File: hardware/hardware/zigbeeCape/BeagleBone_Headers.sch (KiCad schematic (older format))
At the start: 2 parts, among them U4 BeagleBone_P8, U5 BeagleBone_P9

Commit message: Fixing Git issue
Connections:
- net LAN_Heartbeat: now also U5.41 (GPIO_20); no longer U5.15 (GPIO_48)
- net Network_Connect: now also U5.15 (GPIO_48); no longer U5.41 (GPIO_20)
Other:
- note removed: "Random GPIO pin chozen."
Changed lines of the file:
@@
 	1    0    0    -1
 $EndComp
-Text HLabel 5300 2250 0    50   Input ~ 0
+Text HLabel 5650 2250 0    50   Input ~ 0
 BeagleBone_Reset
-Text HLabel 4700 850  0    50   Output ~ 0
+Text HLabel 7300 1550 2    50   Output ~ 0
 LAN_Heartbeat
-Text HLabel 4700 950  0    50   Input ~ 0
+Text HLabel 7300 1650 2    50   Input ~ 0
 Network_Connect
-Text HLabel 5250 3650 0    50   Input ~ 0
+Text HLabel 5650 3650 0    50   Input ~ 0
 UART_TX
-Text HLabel 7500 3150 2    50   Input ~ 0
+Text HLabel 7250 3150 2    50   Input ~ 0
 SPI_MISO
-Text HLabel 7500 3250 2    50   Output ~ 0
+Text HLabel 7250 3250 2    50   Output ~ 0
 SPI_MOSI
-Text HLabel 7500 3350 2    50   Output ~ 0
+Text HLabel 7250 3350 2    50   Output ~ 0
 SPI_CS
-Text HLabel 7500 3050 2    50   Output ~ 0
+Text HLabel 7250 3050 2    50   Output ~ 0
 SPI_CLK
-Text HLabel 7500 3950 2    50   Output ~ 0
+Text HLabel 7250 3950 2    50   Output ~ 0
 I2C2_SCL
-Text HLabel 7500 3850 2    50   BiDi ~ 0
+Text HLabel 7250 3850 2    50   BiDi ~ 0
 I2C2_SDA
-Wire Wire Line
-	5800 2250 5300 2250
-Text HLabel 5250 3750 0    50   Output ~ 0
+Text HLabel 5650 3750 0    50   Output ~ 0
 UART_RX
-Wire Wire Line
-	5800 3750 5250 3750
-Wire Wire Line
-	5250 3650 5800 3650
-Wire Wire Line
-	7100 3950 7500 3950
-Wire Wire Line
-	7500 3850 7100 3850
-Wire Wire Line
-	7500 3350 7100 3350
-Wire Wire Line
-	7100 3250 7500 3250
-Wire Wire Line
-	7500 3150 7100 3150
-Wire Wire Line
-	7500 3050 7100 3050
-Text Notes 5100 800  0    50   ~ 0
-Random GPIO pin chozen.
-Text Notes 5100 1050 0    50   ~ 0
-Random GPIO pin chozen.
-Wire Wire Line
-	2250 1550 1450 1550
-Wire Wire Line
-	1450 1550 1450 1650
-Wire Wire Line
-	5800 1650 5300 1650
-Wire Wire Line
-	5300 1550 5300 1650
-Wire Wire Line
-	5800 2400 5200 2400
-Wire Wire Line
-	5200 2400 5200 2500
-Connection ~ 5200 2500
 $Comp
 L power:GND #PWR046
 U 1 1 608F7A9D
-P 1450 1800
-F 0 "#PWR046" H 1450 1550 50  0001 C CNN
-F 1 "GND" H 1455 1627 50  0000 C CNN
-F 2 "" H 1450 1800 50  0001 C CNN
-F 3 "" H 1450 1800 50  0001 C CNN
-	1    1450 1800
+P 2050 1750
+F 0 "#PWR046" H 2050 1500 50  0001 C CNN
+F 1 "GND" H 2055 1577 50  0000 C CNN
+F 2 "" H 2050 1750 50  0001 C CNN
+F 3 "" H 2050 1750 50  0001 C CNN
+	1    2050 1750
 	1    0    0    -1
 $EndComp
@@
 L power:GND #PWR047
 U 1 1 608F7F64
-P 4800 2550
-F 0 "#PWR047" H 4800 2300 50  0001 C CNN
-F 1 "GND" H 4805 2377 50  0000 C CNN
-F 2 "" H 4800 2550 50  0001 C CNN
-F 3 "" H 4800 2550 50  0001 C CNN
-	1    4800 2550
+P 5650 2950
+F 0 "#PWR047" H 5650 2700 50  0001 C CNN
+F 1 "GND" H 5655 2777 50  0000 C CNN
+F 2 "" H 5650 2950 50  0001 C CNN
+F 3 "" H 5650 2950 50  0001 C CNN
+	1    5650 2950
 	1    0    0    -1
 $EndComp
@@
 L power:+3.3V #PWR048
 U 1 1 608FAB4C
-P 5300 1500
-F 0 "#PWR048" H 5300 1350 50  0001 C CNN
-F 1 "+3.3V" H 5315 1673 50  0000 C CNN
-F 2 "" H 5300 1500 50  0001 C CNN
-F 3 "" H 5300 1500 50  0001 C CNN
-	1    5300 1500
+P 5650 1450
+F 0 "#PWR048" H 5650 1300 50  0001 C CNN
+F 1 "+3.3V" H 5665 1623 50  0000 C CNN
+F 2 "" H 5650 1450 50  0001 C CNN
+F 3 "" H 5650 1450 50  0001 C CNN
+	1    5650 1450
 	1    0    0    -1
 $EndComp
@@
 BeagleBone Headers
 Wire Wire Line
-	5300 1550 5800 1550
-Wire Wire Line
-	5300 1500 5300 1550
-Connection ~ 5300 1550
-Wire Wire Line
-	5200 2500 5800 2500
-Wire Wire Line
-	5800 2900 5200 2900
-Wire Wire Line
-	5200 2900 5200 2800
-Wire Wire Line
-	5800 2800 5200 2800
-Connection ~ 5200 2800
-Wire Wire Line
-	5200 2800 5200 2700
-Wire Wire Line
-	5800 2700 5200 2700
-Connection ~ 5200 2700
-Wire Wire Line
-	5200 2700 5200 2600
-Wire Wire Line
-	5800 2600 5200 2600
-Connection ~ 5200 2600
-Wire Wire Line
-	5200 2600 5200 2500
-Wire Wire Line
-	5200 2400 4800 2400
-Wire Wire Line
-	4800 2400 4800 2550
-Connection ~ 5200 2400
-Wire Wire Line
-	7350 1650 7350 850
-Wire Wire Line
-	4700 850  7350 850
-Wire Wire Line
-	7100 1650 7350 1650
-Wire Wire Line
-	7100 1550 7250 1550
-Wire Wire Line
-	7250 1550 7250 950
-Wire Wire Line
-	4700 950  7250 950
-Wire Wire Line
-	1450 1650 1450 1800
-Wire Wire Line
-	1450 1650 2250 1650
-Connection ~ 1450 1650
+	5800 1550 5650 1550
+Wire Wire Line
+	5650 1550 5650 1450
+Wire Wire Line
+	5800 1650 5650 1650
+Wire Wire Line
+	5650 1650 5650 1550
+Connection ~ 5650 1550
+Wire Wire Line
+	5800 2250 5650 2250
+Wire Wire Line
+	5800 2900 5650 2900
+Wire Wire Line
+	5650 2900 5650 2950
+Wire Wire Line
+	5800 2800 5650 2800
+Wire Wire Line
+	5650 2800 5650 2900
+Connection ~ 5650 2900
+Wire Wire Line
+	5800 2700 5650 2700
+Wire Wire Line
+	5650 2700 5650 2800
+Connection ~ 5650 2800
+Wire Wire Line
+	5800 2600 5650 2600
+Wire Wire Line
+	5650 2600 5650 2700
+Connection ~ 5650 2700
+Wire Wire Line
+	5800 2500 5650 2500
+Wire Wire Line
+	5650 2500 5650 2600
+Connection ~ 5650 2600
+Wire Wire Line
+	5800 2400 5650 2400
+Wire Wire Line
+	5650 2400 5650 2500
+Connection ~ 5650 2500
+Wire Wire Line
+	5650 3650 5800 3650
+Wire Wire Line
+	5800 3750 5650 3750
+Wire Wire Line
+	7100 3950 7250 3950
+Wire Wire Line
+	7250 3850 7100 3850
+Wire Wire Line
+	7250 3350 7100 3350
+Wire Wire Line
+	7250 3250 7100 3250
+Wire Wire Line
+	7250 3150 7100 3150
+Wire Wire Line
+	7250 3050 7100 3050
+Wire Wire Line
+	7100 1650 7300 1650
+Wire Wire Line
+	7100 1550 7300 1550
+Wire Wire Line
+	2250 1650 2050 1650
+Wire Wire Line
+	2050 1650 2050 1750
+Wire Wire Line
+	2250 1550 2050 1550
+Wire Wire Line
+	2050 1550 2050 1650
+Connection ~ 2050 1650
 $EndSCHEMATC

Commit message: Completed BOM except unlabled DNM parts, labled in red. Completed footprint association except onboard antenae
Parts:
- U4, U5: footprint (none) -> Connector_PinHeader_2.54mm:PinHeader_2x23_P2.54mm_Vertical
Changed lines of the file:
@@
 F 0 "U4" H 2900 6815 50  0000 C CNN
 F 1 "BeagleBone_P8" H 2900 6724 50  0000 C CNN
-F 2 "" H 3500 6800 50  0001 C CNN
+F 2 "Connector_PinHeader_2.54mm:PinHeader_2x23_P2.54mm_Vertical" H 3500 6800 50  0001 C CNN
 F 3 "" H 3500 6800 50  0001 C CNN
 	1    2900 4050
@@
 F 0 "U5" H 6450 6815 50  0000 C CNN
 F 1 "BeagleBone_P9" H 6450 6724 50  0000 C CNN
-F 2 "" H 5950 6700 50  0001 C CNN
+F 2 "Connector_PinHeader_2.54mm:PinHeader_2x23_P2.54mm_Vertical" H 5950 6700 50  0001 C CNN
 F 3 "" H 5950 6700 50  0001 C CNN
 	1    6450 4050

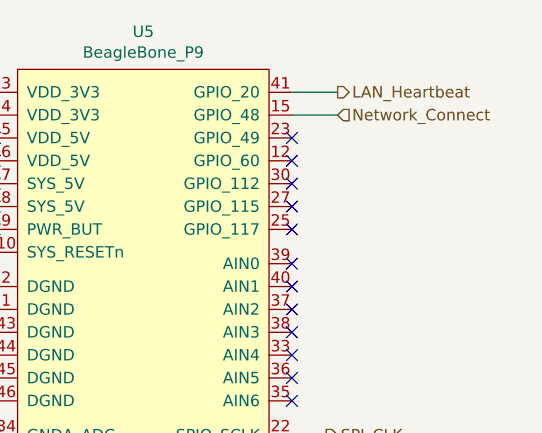
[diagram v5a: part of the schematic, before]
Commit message: Changed min via size, rerouted lan/wifi, cleaned up traces
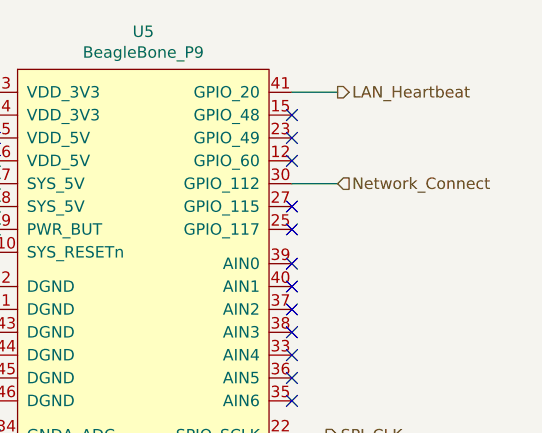
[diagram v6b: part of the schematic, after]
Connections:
- net Network_Connect: now also U5.30 (GPIO_112); no longer U5.15 (GPIO_48)
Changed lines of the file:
@@
 Text HLabel 7300 1550 2    50   Output ~ 0
 LAN_Heartbeat
-Text HLabel 7300 1650 2    50   Input ~ 0
+Text HLabel 7300 1950 2    50   Input ~ 0
 Network_Connect
 Text HLabel 5650 3650 0    50   Input ~ 0
@@
 NoConn ~ 7100 1750
 NoConn ~ 7100 1850
-NoConn ~ 7100 1950
 NoConn ~ 7100 2050
 NoConn ~ 7100 2150
@@
 	7250 3050 7100 3050
 Wire Wire Line
-	7100 1650 7300 1650
-Wire Wire Line
 	7100 1550 7300 1550
 Wire Wire Line
@@
 	2050 1550 2050 1650
 Connection ~ 2050 1650
+Wire Wire Line
+	7100 1950 7300 1950
+NoConn ~ 7100 1650
 $EndSCHEMATC

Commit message: Updated properties for faster BOM generation
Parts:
- U4: Digikey Part Number (none) -> 1528-1365-ND
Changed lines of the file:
@@
 F 2 "Connector_PinHeader_2.54mm:PinHeader_2x23_P2.54mm_Vertical" H 3500 6800 50  0001 C CNN
 F 3 "https://www.digikey.com/en/products/detail/sullins-connector-solutions/PPTC102LFBN-RC/810216" H 3500 6800 50  0001 C CNN
+F 4 "1528-1365-ND" H 2900 4050 50  0001 C CNN "Digikey Part Number"
 	1    2900 4050
 	1    0    0    -1
@@
 F 2 "Connector_PinHeader_2.54mm:PinHeader_2x23_P2.54mm_Vertical" H 5950 6700 50  0001 C CNN
 F 3 "https://www.digikey.com/en/products/detail/sullins-connector-solutions/PPTC102LFBN-RC/810216" H 5950 6700 50  0001 C CNN
+F 4 "~" H 6450 4050 50  0001 C CNN "Digikey Part Number"
 	1    6450 4050
 	1    0    0    -1
